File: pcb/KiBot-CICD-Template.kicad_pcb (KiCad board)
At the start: 4 copper layers, 30.5 x 17.8 mm, 0 parts

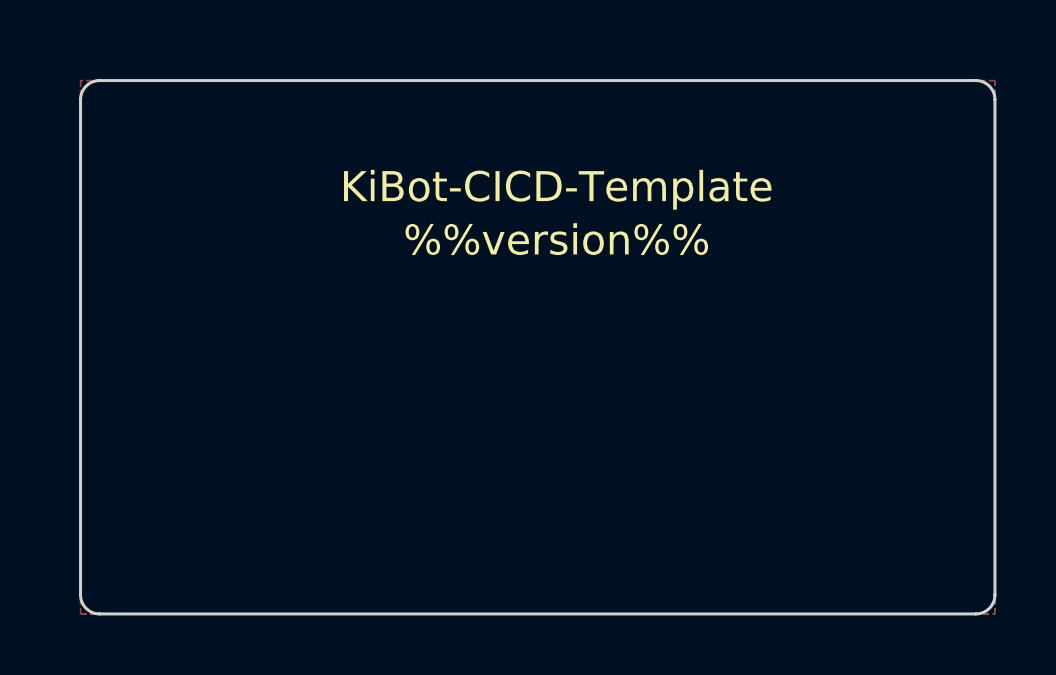
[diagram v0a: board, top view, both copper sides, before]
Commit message: update KiBot
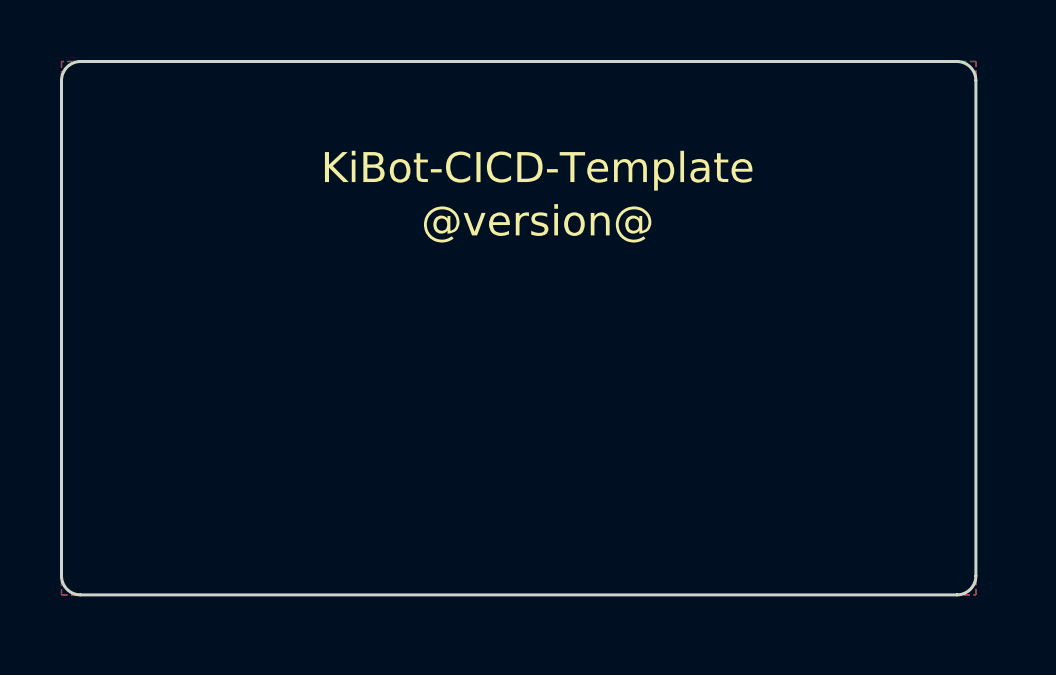
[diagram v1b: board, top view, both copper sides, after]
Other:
- board text added: "@version@"
- board text removed: "%%version%%"
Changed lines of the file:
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@@
   (title_block
     (title "KiBot-CICD-Template")
-    (date "%date%")
-    (rev "%version%")
+    (date "@date@")
+    (rev "@version@")
     (company "nerdyscout")
     (comment 4 "CERN Open Hardware Licence v2.0")
@@
   )
   (net 0 "")
-  (gr_arc (start 138.43 104.775) (mid 138.244013 105.224013) (end 137.795 105.41) (layer "Edge.Cuts") (width 0.1))
-  (gr_arc (start 137.795 87.63) (mid 138.244013 87.815987) (end 138.43 88.265) (layer "Edge.Cuts") (width 0.1))
-  (gr_arc (start 107.95 88.265) (mid 108.135987 87.815987) (end 108.585 87.63) (layer "Edge.Cuts") (width 0.1))
-  (gr_line (start 138.43 104.775) (end 138.43 88.265) (layer "Edge.Cuts") (width 0.1))
-  (gr_line (start 107.95 88.265) (end 107.95 104.775) (layer "Edge.Cuts") (width 0.1))
-  (gr_arc (start 108.585 105.41) (mid 108.135987 105.224013) (end 107.95 104.775) (layer "Edge.Cuts") (width 0.1))
-  (gr_line (start 137.795 105.41) (end 108.585 105.41) (layer "Edge.Cuts") (width 0.1))
-  (gr_line (start 108.585 87.63) (end 137.795 87.63) (layer "Edge.Cuts") (width 0.1))
-  (gr_text "%%version%%" (at 123.825 92.964) (layer "F.SilkS")
+  (gr_arc (start 137.794999 104.139999) (mid 137.609012 104.589012) (end 137.159999 104.774999) (layer "Edge.Cuts") (width 0.1))
+  (gr_arc (start 137.159999 86.994999) (mid 137.609012 87.180986) (end 137.794999 87.629999) (layer "Edge.Cuts") (width 0.1))
+  (gr_arc (start 107.314999 87.629999) (mid 107.500986 87.180986) (end 107.949999 86.994999) (layer "Edge.Cuts") (width 0.1))
+  (gr_line (start 137.794999 104.139999) (end 137.794999 87.629999) (layer "Edge.Cuts") (width 0.1))
+  (gr_line (start 107.314999 87.629999) (end 107.314999 104.139999) (layer "Edge.Cuts") (width 0.1))
+  (gr_arc (start 107.949999 104.774999) (mid 107.500986 104.589012) (end 107.314999 104.139999) (layer "Edge.Cuts") (width 0.1))
+  (gr_line (start 137.159999 104.774999) (end 107.949999 104.774999) (layer "Edge.Cuts") (width 0.1))
+  (gr_line (start 107.949999 86.994999) (end 137.159999 86.994999) (layer "Edge.Cuts") (width 0.1))
+  (gr_text "@version@" (at 123.189999 92.328999) (layer "F.SilkS")
     (effects (font (size 1 1) (thickness 0.25)))
   )
-  (gr_text "KiBot-CICD-Template" (at 123.825 91.186) (layer "F.SilkS")
+  (gr_text "KiBot-CICD-Template" (at 123.189999 90.550999) (layer "F.SilkS")
     (effects (font (size 1 1) (thickness 0.25)))
   )
   (dimension (type aligned) (layer "Dwgs.User")
-    (pts (xy 109.22 87.63) (xy 109.22 105.41))
+    (pts (xy 108.584999 86.994999) (xy 108.584999 104.774999))
     (height 5.08)
-    (gr_text "17.7800 mm" (at 102.99 96.52 90) (layer "Dwgs.User")
+    (gr_text "17.7800 mm" (at 102.354999 95.884999 90) (layer "Dwgs.User")
       (effects (font (size 1 1) (thickness 0.15)))
     )
@@
   )
   (dimension (type aligned) (layer "Dwgs.User")
-    (pts (xy 107.95 88.9) (xy 138.43 88.9))
+    (pts (xy 107.314999 88.264999) (xy 137.794999 88.264999))
     (height -5.08)
-    (gr_text "30.4800 mm" (at 123.19 82.67) (layer "Dwgs.User")
+    (gr_text "30.4800 mm" (at 122.554999 82.034999) (layer "Dwgs.User")
       (effects (font (size 1 1) (thickness 0.15)))
     )
@@
     (polygon
       (pts
-        (xy 107.95 87.63)
-        (xy 107.95 105.41)
-        (xy 138.43 105.41)
-        (xy 138.43 87.63)
+        (xy 107.314999 86.994999)
+        (xy 107.314999 104.774999)
+        (xy 137.794999 104.774999)
+        (xy 137.794999 86.994999)
       )
     )
@@
     (polygon
       (pts
-        (xy 107.95 87.63)
-        (xy 138.43 87.63)
-        (xy 138.43 105.41)
-        (xy 107.95 105.41)
+        (xy 107.314999 86.994999)
+        (xy 137.794999 86.994999)
+        (xy 137.794999 104.774999)
+        (xy 107.314999 104.774999)
       )
     )
@@
     (polygon
       (pts
-        (xy 107.95 87.63)
-        (xy 138.43 87.63)
-        (xy 138.43 105.41)
-        (xy 107.95 105.41)
+        (xy 107.314999 86.994999)
+        (xy 137.794999 86.994999)
+        (xy 137.794999 104.774999)
+        (xy 107.314999 104.774999)
       )
     )
@@
     (polygon
       (pts
-        (xy 107.95 87.63)
-        (xy 107.95 105.41)
-        (xy 138.43 105.41)
-        (xy 138.43 87.63)
+        (xy 107.314999 86.994999)
+        (xy 107.314999 104.774999)
+        (xy 137.794999 104.774999)
+        (xy 137.794999 86.994999)
       )
     )

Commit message: fix string replace
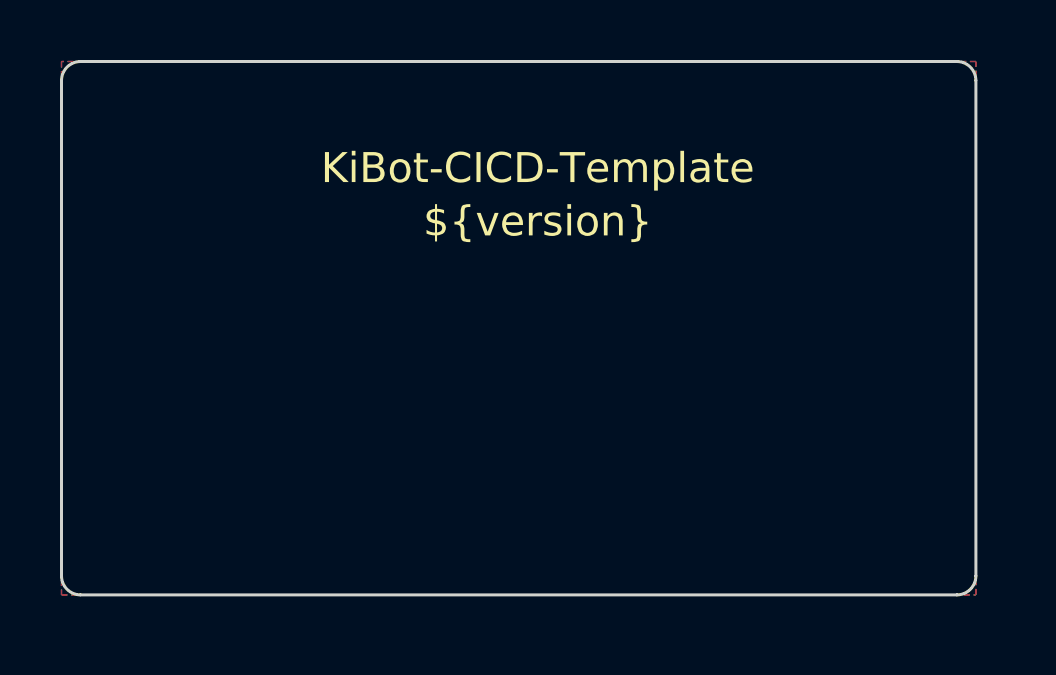
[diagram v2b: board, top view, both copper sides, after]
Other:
- board text added: "${version}"
- board text removed: "@version@"
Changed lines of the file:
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@@
   (title_block
     (title "KiBot-CICD-Template")
-    (date "@date@")
-    (rev "@version@")
+    (date "${date}")
+    (rev "${version}")
     (company "nerdyscout")
     (comment 4 "CERN Open Hardware Licence v2.0")
@@
     )
   )
+  (property "Variable" "")
   (net 0 "")
   (gr_arc (start 137.794999 104.139999) (mid 137.609012 104.589012) (end 137.159999 104.774999) (layer "Edge.Cuts") (width 0.1))
@@
   (gr_line (start 137.159999 104.774999) (end 107.949999 104.774999) (layer "Edge.Cuts") (width 0.1))
   (gr_line (start 107.949999 86.994999) (end 137.159999 86.994999) (layer "Edge.Cuts") (width 0.1))
-  (gr_text "@version@" (at 123.189999 92.328999) (layer "F.SilkS")
+  (gr_text "${version}" (at 123.189999 92.328999) (layer "F.SilkS")
     (effects (font (size 1 1) (thickness 0.25)))
   )

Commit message: update template
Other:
- board text added: "${REVISION}"
- board text removed: "${version}"
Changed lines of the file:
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@@
   (title_block
     (title "KiBot-CICD-Template")
-    (date "${date}")
-    (rev "${version}")
-    (company "nerdyscout")
-    (comment 4 "CERN Open Hardware Licence v2.0")
+    (company "@stop_pattern")
   )
   (layers
@@
   (gr_line (start 137.159999 104.774999) (end 107.949999 104.774999) (layer "Edge.Cuts") (width 0.1))
   (gr_line (start 107.949999 86.994999) (end 137.159999 86.994999) (layer "Edge.Cuts") (width 0.1))
-  (gr_text "${version}" (at 123.189999 92.328999) (layer "F.SilkS")
+  (gr_text "${REVISION}" (at 123.189999 92.328999) (layer "F.SilkS")
     (effects (font (size 1 1) (thickness 0.25)))
   )
